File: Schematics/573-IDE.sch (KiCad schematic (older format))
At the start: 20 parts, among them CN15 B4P-VH, CN2I ATA-IDE, CN2P Intergrated IDE Connector

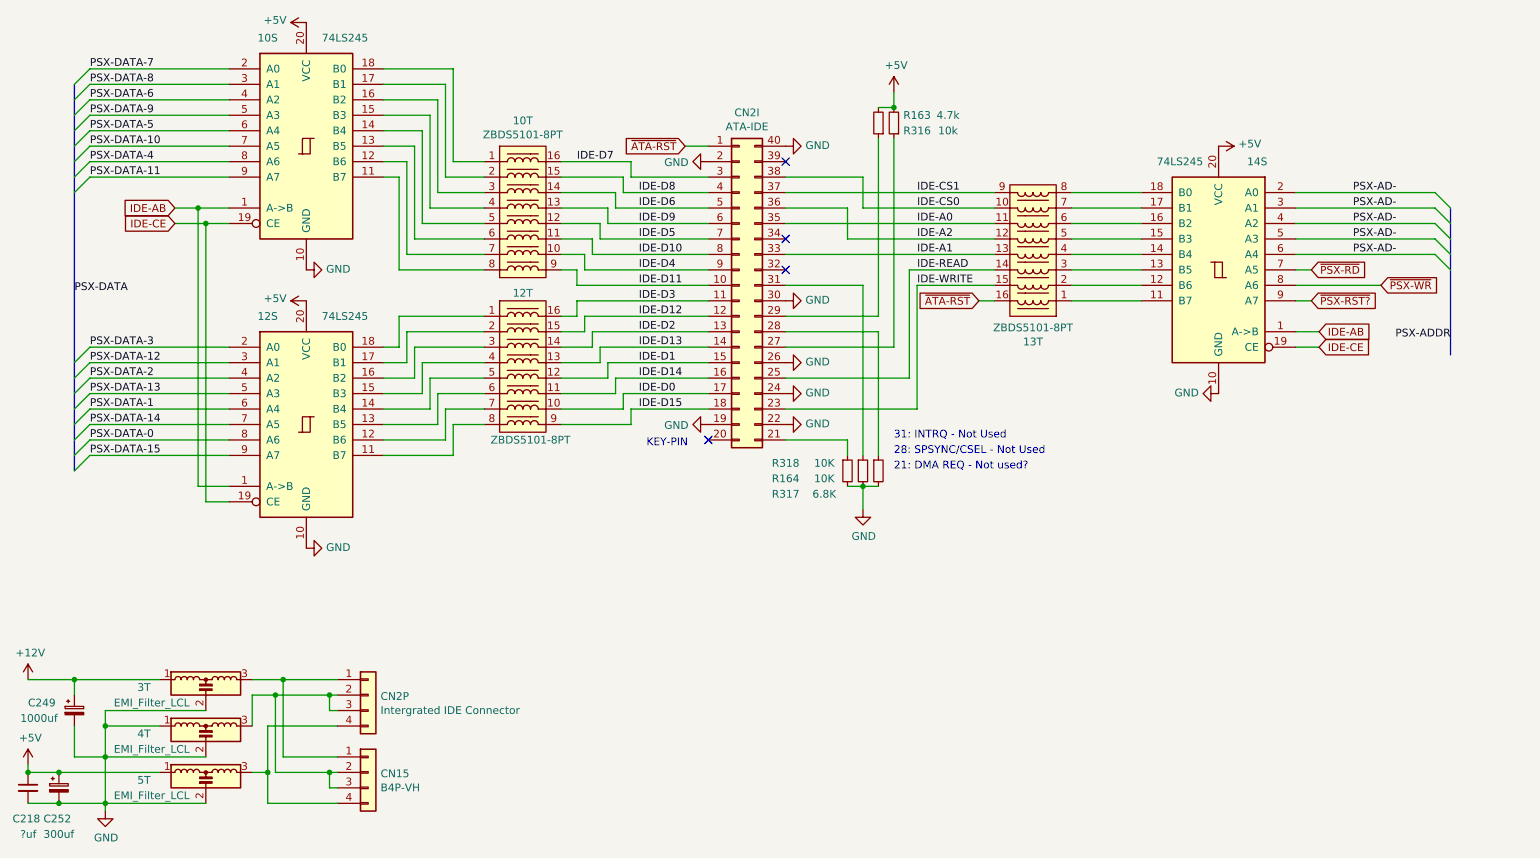
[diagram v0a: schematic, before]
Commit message: Added GE675-PWB(A)
IO Board for Fisherman's Bait 3
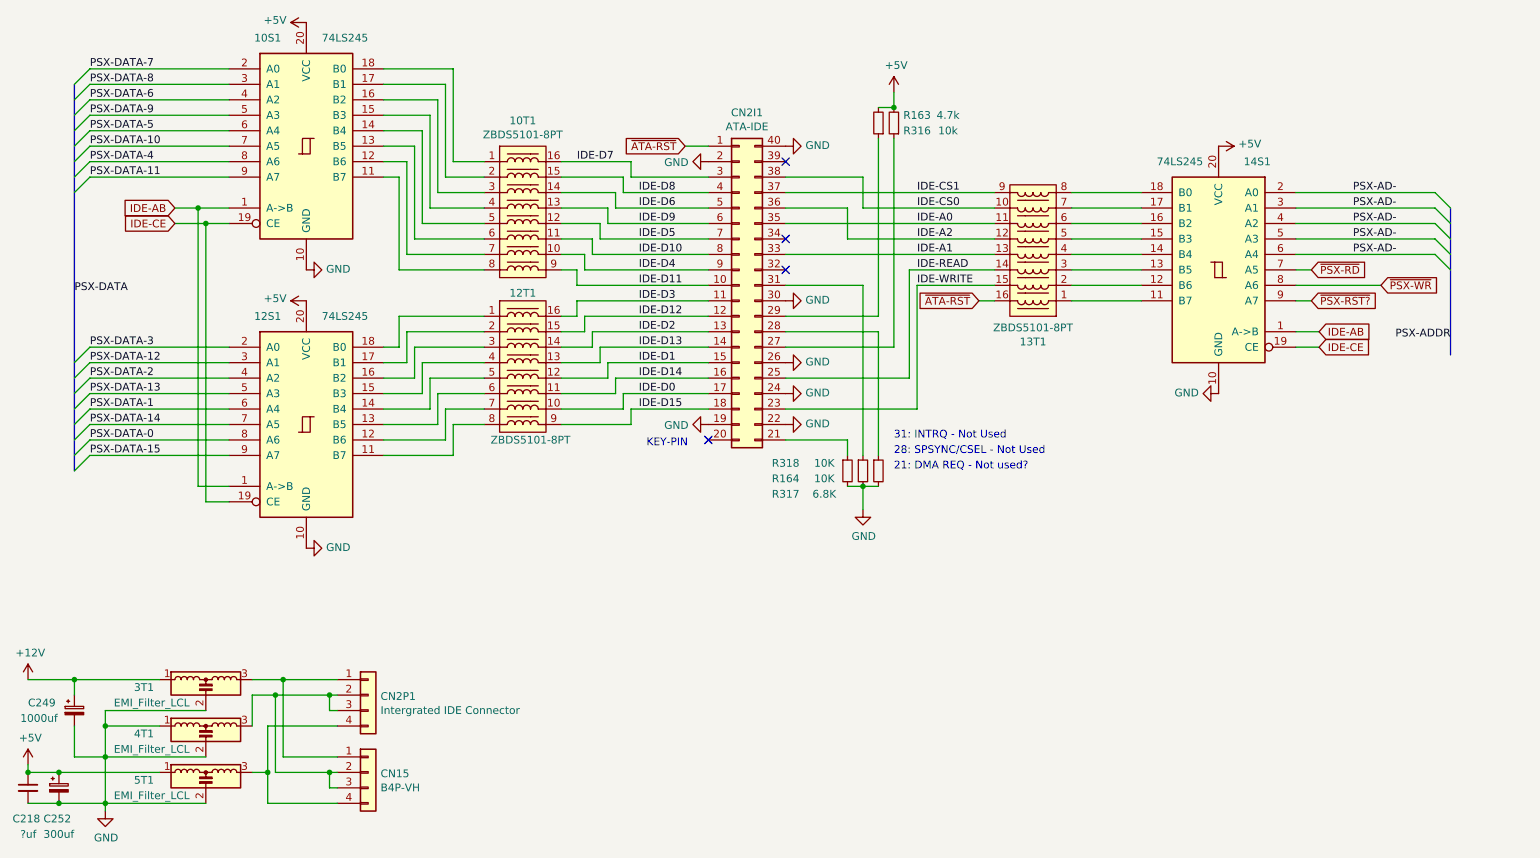
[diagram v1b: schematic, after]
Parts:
- renumbered 10S to 10S1, 10T to 10T1, 12S to 12S1, 12T to 12T1, 13T to 13T1, 14S to 14S1, 3T to 3T1, 4T to 4T1, 5T to 5T1, CN2I to CN2I1, CN2P to CN2P1
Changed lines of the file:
@@
 $EndDescr
 $Comp
-L Connector_Generic:Conn_02x20_Counter_Clockwise CN2I
+L Connector_Generic:Conn_02x20_Counter_Clockwise CN2I1
 U 1 1 6257E3E3
 P 5900 2900
-F 0 "CN2I" H 5950 4017 50  0000 C CNN
+F 0 "CN2I1" H 5950 4017 50  0000 C CNN
 F 1 "ATA-IDE" H 5950 3926 50  0000 C CNN
 F 2 "Connector_PinSocket_2.54mm:PinSocket_2x20_P2.54mm_Vertical" H 5900 2900 50  0001 C CNN
@@
 AR Path="/637479AE/6258B49D" Ref="36A?"  Part="1"
 AR Path="/63647603/6258B49D" Ref="36A?"  Part="1"
-AR Path="/6257BCAC/6258B49D" Ref="13T"  Part="1"
-F 0 "13T" H 7800 3265 50  0000 C CNN
+AR Path="/6257BCAC/6258B49D" Ref="13T1"  Part="1"
+F 0 "13T1" H 7800 3265 50  0000 C CNN
 F 1 "ZBDS5101-8PT" H 7800 3174 50  0000 C CNN
 F 2 "Package_SO:SOIC-16_4.55x10.3mm_P1.27mm" H 7800 2150 50  0001 C CNN
@@
 AR Path="/637479AE/625ACB61" Ref="13T?"  Part="1"
 AR Path="/63647603/625ACB61" Ref="13T?"  Part="1"
-AR Path="/6257BCAC/625ACB61" Ref="10T"  Part="1"
-F 0 "10T" H 4500 3065 50  0000 C CNN
+AR Path="/6257BCAC/625ACB61" Ref="10T1"  Part="1"
+F 0 "10T1" H 4500 3065 50  0000 C CNN
 F 1 "ZBDS5101-8PT" H 4500 2974 50  0000 C CNN
 F 2 "Package_SO:SOIC-16_4.55x10.3mm_P1.27mm" H 4500 1950 50  0001 C CNN
@@
 AR Path="/637479AE/625DCA0E" Ref="12T?"  Part="1"
 AR Path="/63647603/625DCA0E" Ref="12T?"  Part="1"
-AR Path="/6257BCAC/625DCA0E" Ref="12T"  Part="1"
-F 0 "12T" H 4500 3950 50  0000 C CNN
+AR Path="/6257BCAC/625DCA0E" Ref="12T1"  Part="1"
+F 0 "12T1" H 4500 3950 50  0000 C CNN
 F 1 "ZBDS5101-8PT" H 4550 3000 50  0000 C CNN
 F 2 "Package_SO:SOIC-16_4.55x10.3mm_P1.27mm" H 4500 2950 50  0001 C CNN
@@
 	3700 2200 3600 2200
 $Comp
-L 74xx:74LS245 12S
+L 74xx:74LS245 12S1
 U 1 1 6260754E
 P 3100 3800
-F 0 "12S" H 2850 4500 50  0000 C CNN
+F 0 "12S1" H 2850 4500 50  0000 C CNN
 F 1 "74LS245" H 3350 4500 50  0000 C CNN
 F 2 "Package_SO:SO-20_5.3x12.6mm_P1.27mm" H 3100 3800 50  0001 C CNN
@@
 	3700 3300 3600 3300
 $Comp
-L 74xx:74LS245 10S
+L 74xx:74LS245 10S1
 U 1 1 625F11EF
 P 3100 2000
-F 0 "10S" H 2850 2700 50  0000 C CNN
+F 0 "10S1" H 2850 2700 50  0000 C CNN
 F 1 "74LS245" H 3350 2700 50  0000 C CNN
 F 2 "Package_SO:SO-20_5.3x12.6mm_P1.27mm" H 3100 2000 50  0001 C CNN
@@
 	4050 1500 4050 2100
 $Comp
-L power:GND #PWR?
+L power:GND #PWR0136
 U 1 1 6266AC8F
 P 3100 2800
-F 0 "#PWR?" H 3100 2550 50  0001 C CNN
+F 0 "#PWR0136" H 3100 2550 50  0001 C CNN
 F 1 "GND" V 3105 2672 50  0000 R CNN
 F 2 "" H 3100 2800 50  0001 C CNN
@@
 $EndComp
 $Comp
-L power:GND #PWR?
+L power:GND #PWR0137
 U 1 1 6266B8E2
 P 3100 4600
-F 0 "#PWR?" H 3100 4350 50  0001 C CNN
+F 0 "#PWR0137" H 3100 4350 50  0001 C CNN
 F 1 "GND" V 3105 4472 50  0000 R CNN
 F 2 "" H 3100 4600 50  0001 C CNN
@@
 $EndComp
 $Comp
-L power:+5V #PWR?
+L power:+5V #PWR0138
 U 1 1 6266C3ED
 P 3100 1200
-F 0 "#PWR?" H 3100 1050 50  0001 C CNN
+F 0 "#PWR0138" H 3100 1050 50  0001 C CNN
 F 1 "+5V" V 3115 1328 50  0000 L CNN
 F 2 "" H 3100 1200 50  0001 C CNN
@@
 $EndComp
 $Comp
-L power:+5V #PWR?
+L power:+5V #PWR0139
 U 1 1 6266CEC5
 P 3100 3000
-F 0 "#PWR?" H 3100 2850 50  0001 C CNN
+F 0 "#PWR0139" H 3100 2850 50  0001 C CNN
 F 1 "+5V" V 3115 3128 50  0000 L CNN
 F 2 "" H 3100 3000 50  0001 C CNN
@@
 	2450 4300 2600 4300
 $Comp
-L power:GND #PWR?
+L power:GND #PWR0140
 U 1 1 6267EA3E
 P 5700 2100
-F 0 "#PWR?" H 5700 1850 50  0001 C CNN
+F 0 "#PWR0140" H 5700 1850 50  0001 C CNN
 F 1 "GND" V 5705 1972 50  0000 R CNN
 F 2 "" H 5700 2100 50  0001 C CNN
@@
 PSX-DATA
 $Comp
-L Connector_Generic:Conn_01x04 CN2P
+L Connector_Generic:Conn_01x04 CN2P1
 U 1 1 6271681A
 P 3500 5550
-F 0 "CN2P" H 3580 5542 50  0000 L CNN
+F 0 "CN2P1" H 3580 5542 50  0000 L CNN
 F 1 "Intergrated IDE Connector" H 3580 5451 50  0000 L CNN
 F 2 "" H 3500 5550 50  0001 C CNN
@@
 $EndComp
 $Comp
-L Device:EMI_Filter_LCL 3T
+L Device:EMI_Filter_LCL 3T1
 U 1 1 62721373
 P 2450 5550
-F 0 "3T" H 2050 5600 50  0000 C CNN
+F 0 "3T1" H 2050 5600 50  0000 C CNN
 F 1 "EMI_Filter_LCL" H 2100 5500 50  0000 C CNN
 F 2 "Connector_PinSocket_2.54mm:PinSocket_1x03_P2.54mm_Vertical" V 2450 5550 50  0001 C CNN
@@
 $EndComp
 $Comp
-L Device:EMI_Filter_LCL 4T
+L Device:EMI_Filter_LCL 4T1
 U 1 1 627220C7
 P 2450 5850
-F 0 "4T" H 2050 5900 50  0000 C CNN
+F 0 "4T1" H 2050 5900 50  0000 C CNN
 F 1 "EMI_Filter_LCL" H 2100 5800 50  0000 C CNN
 F 2 "Connector_PinSocket_2.54mm:PinSocket_1x03_P2.54mm_Vertical" V 2450 5850 50  0001 C CNN
@@
 Connection ~ 1800 5950
 $Comp
-L power:GND #PWR?
+L power:GND #PWR0141
 U 1 1 627474C7
 P 1800 6300
-F 0 "#PWR?" H 1800 6050 50  0001 C CNN
+F 0 "#PWR0141" H 1800 6050 50  0001 C CNN
 F 1 "GND" H 1805 6127 50  0000 C CNN
 F 2 "" H 1800 6300 50  0001 C CNN
@@
 $EndComp
 $Comp
-L power:+5V #PWR?
+L power:+5V #PWR0142
 U 1 1 627482D7
 P 1300 6000
-F 0 "#PWR?" H 1300 5850 50  0001 C CNN
+F 0 "#PWR0142" H 1300 5850 50  0001 C CNN
 F 1 "+5V" H 1315 6173 50  0000 C CNN
 F 2 "" H 1300 6000 50  0001 C CNN
@@
 $EndComp
 $Comp
-L power:+12V #PWR?
+L power:+12V #PWR0143
 U 1 1 6275AE71
 P 1300 5450
-F 0 "#PWR?" H 1300 5300 50  0001 C CNN
+F 0 "#PWR0143" H 1300 5300 50  0001 C CNN
 F 1 "+12V" H 1315 5623 50  0000 C CNN
 F 2 "" H 1300 5450 50  0001 C CNN
@@
 	2850 6050 2850 6250
 $Comp
-L Device:EMI_Filter_LCL 5T
+L Device:EMI_Filter_LCL 5T1
 U 1 1 62722E5F
 P 2450 6150
-F 0 "5T" H 2050 6200 50  0000 C CNN
+F 0 "5T1" H 2050 6200 50  0000 C CNN
 F 1 "EMI_Filter_LCL" H 2100 6100 50  0000 C CNN
 F 2 "Connector_PinSocket_2.54mm:PinSocket_1x03_P2.54mm_Vertical" V 2450 6150 50  0001 C CNN
@@
 Connection ~ 1600 5450
 $Comp
-L power:GND #PWR?
+L power:GND #PWR0144
 U 1 1 628550BA
 P 5700 3800
-F 0 "#PWR?" H 5700 3550 50  0001 C CNN
+F 0 "#PWR0144" H 5700 3550 50  0001 C CNN
 F 1 "GND" V 5705 3672 50  0000 R CNN
 F 2 "" H 5700 3800 50  0001 C CNN
@@
 $EndComp
 $Comp
-L power:GND #PWR?
+L power:GND #PWR0145
 U 1 1 62888CC1
 P 6700 4350
-F 0 "#PWR?" H 6700 4100 50  0001 C CNN
+F 0 "#PWR0145" H 6700 4100 50  0001 C CNN
 F 1 "GND" H 6705 4177 50  0000 C CNN
 F 2 "" H 6700 4350 50  0001 C CNN
@@
 21: DMA REQ - Not used?
 $Comp
-L power:GND #PWR?
+L power:GND #PWR0146
 U 1 1 628D7A7E
 P 6200 3800
-F 0 "#PWR?" H 6200 3550 50  0001 C CNN
+F 0 "#PWR0146" H 6200 3550 50  0001 C CNN
 F 1 "GND" V 6205 3672 50  0000 R CNN
 F 2 "" H 6200 3800 50  0001 C CNN
@@
 $EndComp
 $Comp
-L power:GND #PWR?
+L power:GND #PWR0147
 U 1 1 628E49C7
 P 6200 3600
-F 0 "#PWR?" H 6200 3350 50  0001 C CNN
+F 0 "#PWR0147" H 6200 3350 50  0001 C CNN
 F 1 "GND" V 6205 3472 50  0000 R CNN
 F 2 "" H 6200 3600 50  0001 C CNN
@@
 $EndComp
 $Comp
-L power:GND #PWR?
+L power:GND #PWR0148
 U 1 1 628E4FA1
 P 6200 3400
-F 0 "#PWR?" H 6200 3150 50  0001 C CNN
+F 0 "#PWR0148" H 6200 3150 50  0001 C CNN
 F 1 "GND" V 6205 3272 50  0000 R CNN
 F 2 "" H 6200 3400 50  0001 C CNN
@@
 	6900 3300 6900 1950
 $Comp
-L power:+5V #PWR?
+L power:+5V #PWR0149
 U 1 1 629BD0BD
 P 6900 1650
-F 0 "#PWR?" H 6900 1500 50  0001 C CNN
+F 0 "#PWR0149" H 6900 1500 50  0001 C CNN
 F 1 "+5V" H 6915 1823 50  0000 C CNN
 F 2 "" H 6900 1650 50  0001 C CNN
@@
 	6800 3100 6800 1950
 $Comp
-L power:GND #PWR?
+L power:GND #PWR0150
 U 1 1 629D4F99
 P 6200 3000
-F 0 "#PWR?" H 6200 2750 50  0001 C CNN
+F 0 "#PWR0150" H 6200 2750 50  0001 C CNN
 F 1 "GND" V 6205 2872 50  0000 R CNN
 F 2 "" H 6200 3000 50  0001 C CNN
@@
 	6200 2300 7550 2300
 $Comp
-L power:GND #PWR?
+L power:GND #PWR0151
 U 1 1 62AC8AFB
 P 6200 2000
-F 0 "#PWR?" H 6200 1750 50  0001 C CNN
+F 0 "#PWR0151" H 6200 1750 50  0001 C CNN
 F 1 "GND" V 6205 1872 50  0000 R CNN
 F 2 "" H 6200 2000 50  0001 C CNN
@@
 	8050 2500 8500 2500
 $Comp
-L 74xx:74LS245 14S
+L 74xx:74LS245 14S1
 U 1 1 62B44F65
 P 9000 2800
-F 0 "14S" H 8750 3500 50  0000 C CNN
+F 0 "14S1" H 8750 3500 50  0000 C CNN
 F 1 "74LS245" H 9250 3500 50  0000 C CNN
 F 2 "Package_SO:SO-20_5.3x12.6mm_P1.27mm" H 9000 2800 50  0001 C CNN
@@
 $EndComp
 $Comp
-L power:GND #PWR?
+L power:GND #PWR0152
 U 1 1 62B44F6F
 P 9000 3600
-F 0 "#PWR?" H 9000 3350 50  0001 C CNN
+F 0 "#PWR0152" H 9000 3350 50  0001 C CNN
 F 1 "GND" V 9005 3472 50  0000 R CNN
 F 2 "" H 9000 3600 50  0001 C CNN
@@
 $EndComp
 $Comp
-L power:+5V #PWR?
+L power:+5V #PWR0153
 U 1 1 62B44F79
 P 9000 2000
-F 0 "#PWR?" H 9000 1850 50  0001 C CNN
+F 0 "#PWR0153" H 9000 1850 50  0001 C CNN
 F 1 "+5V" V 9015 2128 50  0000 L CNN
 F 2 "" H 9000 2000 50  0001 C CNN

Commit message: Fixed bugs
IDE Retrace, PCMCIA checked
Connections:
- net +5V: now also 14S1.1 (A->B)
- net GND: now also 14S1.19 (CE)
- net IDE-A0: now also 13T1.14; no longer 13T1.11
- net IDE-A1: now also 13T1.12; no longer 13T1.13
- net IDE-A2: now also 13T1.13; no longer 13T1.12
- net IDE-AB: no longer 14S1.1 (A->B)
- net IDE-CE: no longer 14S1.19 (CE)
- net IDE-CS0: now also 13T1.15, CN2I1.37 (Pin_37); no longer 13T1.10, CN2I1.38 (Pin_38)
- net IDE-CS1: now also 13T1.16, CN2I1.38 (Pin_38); no longer 13T1.9, CN2I1.37 (Pin_37)
- net IDE-READ: now also 13T1.11; no longer 13T1.14
- net IDE-WRITE: now also 13T1.10; no longer 13T1.15
- net ~ATA-RST: now also 13T1.9; no longer 13T1.16
- removed net PSX-AD-: 14S1.2 (A0), 14S1.3 (A1), 14S1.4 (A2), 14S1.5 (A3), 14S1.6 (A4)
- net PSX-DATA-0 renamed IO-DATA-0
- net PSX-DATA-1 renamed IO-DATA-1
- net PSX-DATA-10 renamed IO-DATA-10
- net PSX-DATA-11 renamed IO-DATA-11
- net PSX-DATA-12 renamed IO-DATA-12
- net PSX-DATA-13 renamed IO-DATA-13
- net PSX-DATA-14 renamed IO-DATA-14
- net PSX-DATA-15 renamed IO-DATA-15
- net PSX-DATA-2 renamed IO-DATA-2
- net PSX-DATA-3 renamed IO-DATA-3
- net PSX-DATA-4 renamed IO-DATA-4
- net PSX-DATA-5 renamed IO-DATA-5
- net PSX-DATA-6 renamed IO-DATA-6
- net PSX-DATA-7 renamed IO-DATA-7
- net PSX-DATA-8 renamed IO-DATA-8
- net PSX-DATA-9 renamed IO-DATA-9
- net ~PSX-RD renamed IO-ADDR-1
- net ~PSX-RST? renamed U17-3
- net ~PSX-WR renamed U17-2
- new net IO-ADDR-2: 14S1.5 (A3)
- new net IO-ADDR-3: 14S1.6 (A4)
- new net ~BUS-RD: 14S1.4 (A2)
- new net ~BUS-WR: 14S1.3 (A1)
- new net ~RESET: 14S1.2 (A0)
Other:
- note added: "CPLD"
- moved on the sheet: 13T1, 14S1

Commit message: 573 specific mostly mapped
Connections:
- net U71-22: now reaches CN2I1.31 (Pin_31), R164.1
- net IDE-AB renamed BUS-~RD
- net IDE-CE renamed U71-34
- net U17-2 renamed U71-2
- net U17-3 renamed U71-3
- net ~RESET renamed IDE-~RST
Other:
- note added: "31: INTRQ maps to"
- note removed: "31: INTRQ - Not Used"
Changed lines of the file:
@@
 28: SPSYNC/CSEL - Not Used\n
 Text Notes 6900 3900 0    50   ~ 0
-31: INTRQ - Not Used
+31: INTRQ maps to
 Wire Wire Line
 	6200 2200 6650 2200
@@
 	8350 2900 8800 2900
 Text GLabel 2250 2400 0    50   Input ~ 0
-IDE-AB
+BUS-~RD
 Text GLabel 2250 2500 0    50   Input ~ 0
-IDE-CE
+U71-34
 Wire Wire Line
 	2450 2500 2250 2500
@@
 Wire Wire Line
 	1300 5450 1600 5450
-Text GLabel 9900 2300 2    50   Input ~ 0
-~RESET
 Wire Wire Line
 	9800 2400 10350 2400
@@
 	6700 3800 6550 3800
 Wire Wire Line
-	6550 3800 6550 2900
+	6550 3800 6550 3400
 Wire Wire Line
 	6700 3800 6700 4000
@@
 	9800 2800 10350 2800
 Text GLabel 10350 3000 2    50   Input ~ 0
-U17-3
+U71-3
 Wire Wire Line
 	9800 3000 10350 3000
 Text GLabel 9900 2900 2    50   Input ~ 0
-U17-2
+U71-2
 Wire Wire Line
 	9900 2900 9800 2900
@@
 Wire Notes Line
 	9850 3100 9850 2850
+Text Notes 10750 3050 0    50   ~ 0
+CPLD
+Text GLabel 9900 2300 2    50   Input ~ 0
+IDE-~RST
+Text GLabel 7350 3400 2    50   Input ~ 0
+U71-22
+Wire Wire Line
+	6550 3400 7350 3400
 Wire Bus Line
 	1600 1600 1600 4100
-Text Notes 10750 3050 0    50   ~ 0
-CPLD
+Connection ~ 6550 3400
+Wire Wire Line
+	6550 3400 6550 2900
 $EndSCHEMATC
